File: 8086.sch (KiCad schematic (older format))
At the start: 11 parts, among them SW1 SW_Push, U1 8086_Min_Mode, U2 74LS373, U3 74LS373, U4 74LS373, U5 74LS244, U6 74LS245, U7 74LS245

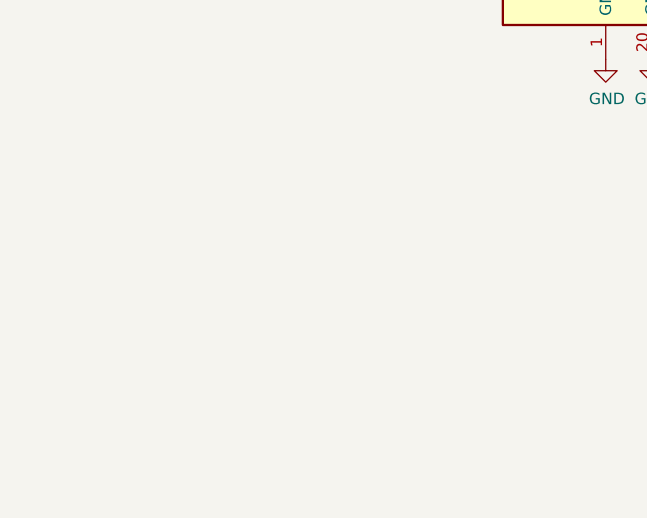
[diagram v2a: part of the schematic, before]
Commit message: integrated clock
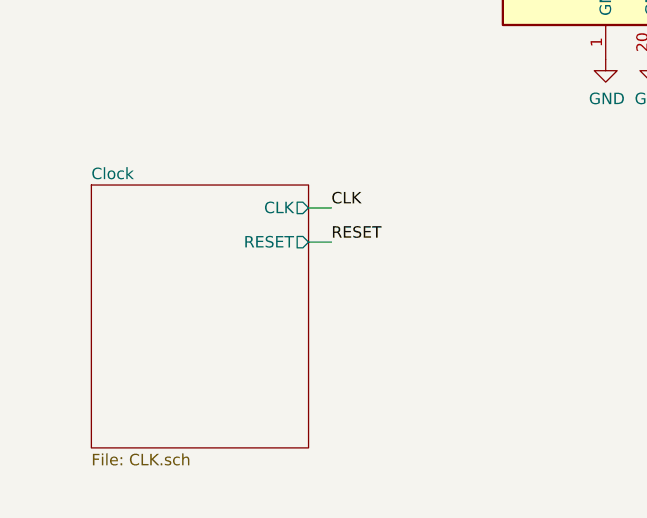
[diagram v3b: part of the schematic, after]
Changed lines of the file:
@@
 $Descr A4 11693 8268
 encoding utf-8
-Sheet 1 1
+Sheet 1 2
 Title ""
 Date ""
@@
 Wire Wire Line
 	10900 2750 10150 2750
+Connection ~ 10150 2750
+$Sheet
+S 800  5050 950  1150
+U 60790D94
+F0 "Clock" 50
+F1 "CLK.sch" 50
+F2 "CLK" O R 1750 5150 50
+F3 "RESET" O R 1750 5300 50
+$EndSheet
+Wire Wire Line
+	1750 5150 1850 5150
+Wire Wire Line
+	1750 5300 1850 5300
 Wire Bus Line
 	9250 2850 9250 5500
@@
 Wire Bus Line
 	4100 1550 4100 3600
-Connection ~ 10150 2750
+Text Label 1850 5150 0    50   ~ 0
+CLK
+Text Label 1850 5300 0    50   ~ 0
+RESET
 $EndSCHEMATC

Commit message: Some minor changes
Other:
- moved on the sheet: C1, D1, R1, SW1, U1

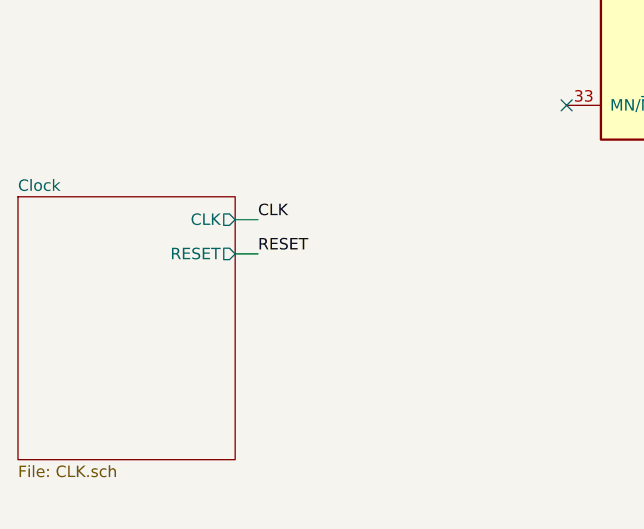
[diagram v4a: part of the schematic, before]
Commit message: Add files via upload
added ready pin to clk
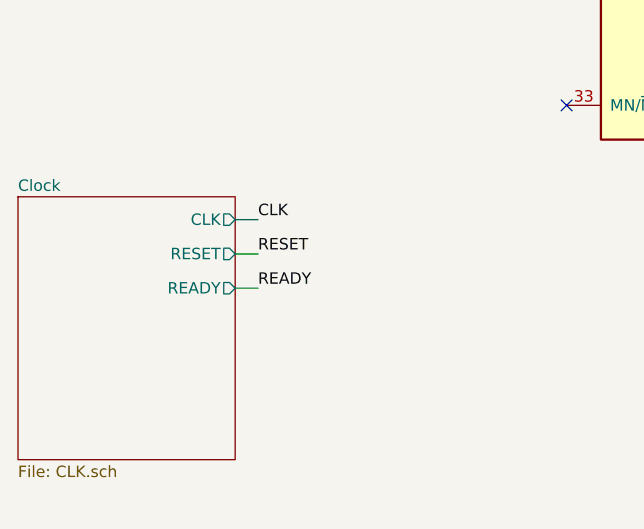
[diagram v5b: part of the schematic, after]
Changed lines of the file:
@@
 F2 "CLK" O R 1750 5150 50
 F3 "RESET" O R 1750 5300 50
+F4 "READY" O R 1750 5450 50
 $EndSheet
 Wire Wire Line
@@
 Text Label 1850 5300 0    50   ~ 0
 RESET
+Wire Wire Line
+	1750 5450 1850 5450
 Wire Bus Line
 	9250 2850 9250 5500
@@
 Wire Bus Line
 	4850 2000 4850 4050
+Text Label 1850 5450 0    50   ~ 0
+READY
 $EndSCHEMATC

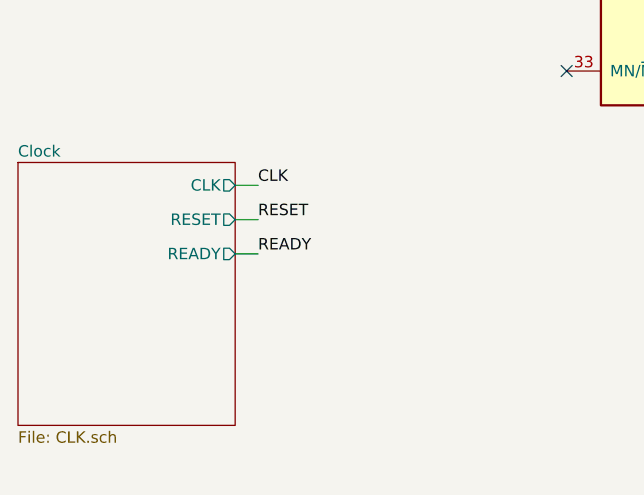
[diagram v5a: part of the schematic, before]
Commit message: Add files via upload
Added PCLK as a hierarchical label to CLK
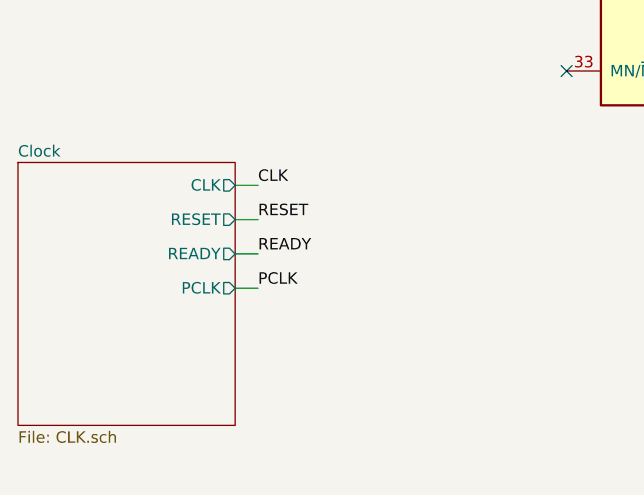
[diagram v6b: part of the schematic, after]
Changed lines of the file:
@@
 F3 "RESET" O R 1750 5300 50
 F4 "READY" O R 1750 5450 50
+F5 "PCLK" O R 1750 5600 50
 $EndSheet
 Wire Wire Line
@@
 Wire Wire Line
 	1750 5450 1850 5450
+Text Label 1850 5450 0    50   ~ 0
+READY
+Wire Wire Line
+	1750 5600 1850 5600
 Wire Bus Line
 	9250 2850 9250 5500
@@
 Wire Bus Line
 	4850 2000 4850 4050
-Text Label 1850 5450 0    50   ~ 0
-READY
+Text Label 1850 5600 0    50   ~ 0
+PCLK
 $EndSCHEMATC
